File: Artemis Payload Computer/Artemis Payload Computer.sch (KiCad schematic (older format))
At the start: 0 parts

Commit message: complete redo hehe
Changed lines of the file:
@@
 $Descr A4 11693 8268
 encoding utf-8
-Sheet 1 2
+Sheet 1 6
 Title ""
 Date ""
@@
 Wire Wire Line
 	7450 1040 7220 1040
+$Sheet
+S 2400 2700 2650 1350
+U 60403E20
+F0 "Teensy3.2" 50
+F1 "Teensy3.sch" 50
+$EndSheet
+$Sheet
+S 5950 2700 1250 700
+U 60404056
+F0 "IMU" 50
+F1 "IMU.sch" 50
+$EndSheet
+$Sheet
+S 5950 3800 1250 650
+U 60404167
+F0 "BMP280" 50
+F1 "BMP280.sch" 50
+$EndSheet
+$Sheet
+S 6000 4950 1200 650
+U 60404A5A
+F0 "Power Supply" 50
+F1 "Power Supply.sch" 50
+$EndSheet
 $EndSCHEMATC

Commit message: ready for testing...
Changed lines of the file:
@@
 F0 "Teensy3.2" 50
 F1 "Teensy3.sch" 50
+F2 "SCL0" I R 5050 3100 50
+F3 "SDA0" I R 5050 3550 50
 $EndSheet
 $Sheet
@@
 F0 "IMU" 50
 F1 "IMU.sch" 50
+F2 "SCL0" I L 5950 2850 50
+F3 "SDA0" I L 5950 3150 50
 $EndSheet
 $Sheet
@@
 F0 "BMP280" 50
 F1 "BMP280.sch" 50
+F2 "SCL0" I L 5950 4000 50
+F3 "SDA0" I L 5950 4200 50
 $EndSheet
 $Sheet

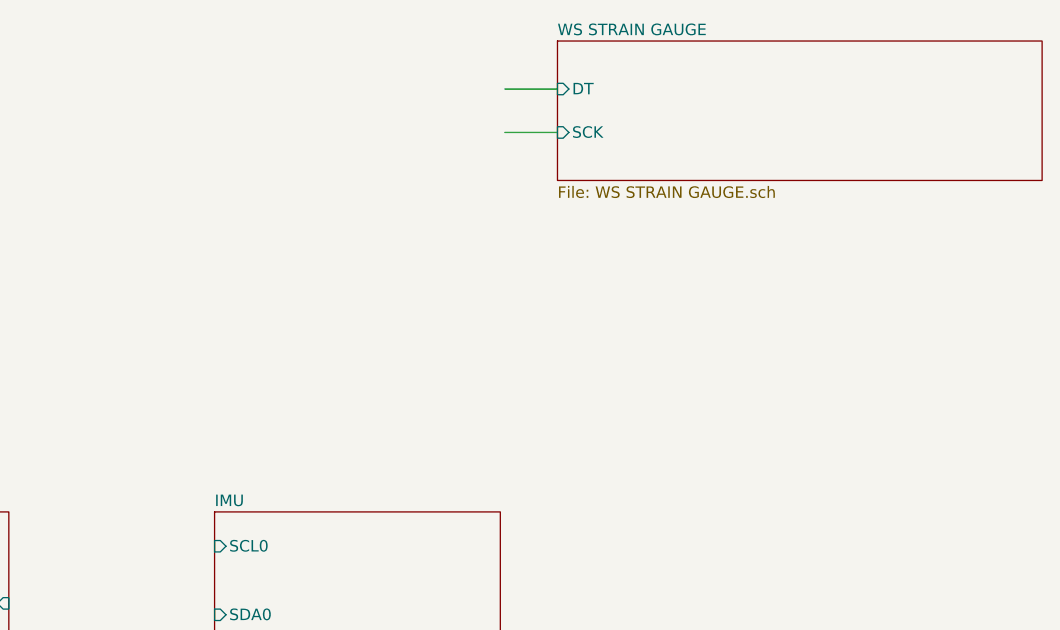
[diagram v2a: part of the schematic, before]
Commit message: Fixed Strain Gauge Footprint
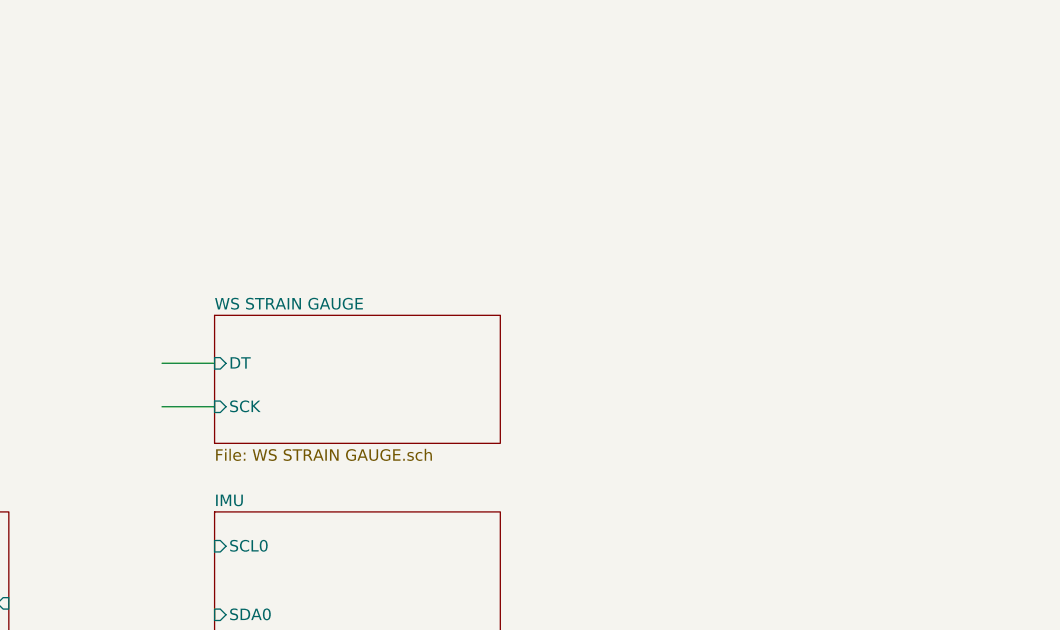
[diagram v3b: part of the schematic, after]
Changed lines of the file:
@@
 $EndDescr
 $Sheet
-S 7450 640  2120 610
+S 5950 1840 1250 560
 U 603A9D0E
 F0 "WS STRAIN GAUGE" 50
 F1 "WS STRAIN GAUGE.sch" 50
-F2 "DT" I L 7450 850 50
-F3 "SCK" I L 7450 1040 50
+F2 "DT" I L 5950 2050 50
+F3 "SCK" I L 5950 2240 50
 $EndSheet
 Wire Wire Line
-	7450 850  7220 850
+	5950 2050 5720 2050
 Wire Wire Line
-	7450 1040 7220 1040
+	5950 2240 5720 2240
 $Sheet
 S 2400 2700 2650 1350

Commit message: big commit, sorry. sd card needs finishing
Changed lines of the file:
@@
 $Descr A4 11693 8268
 encoding utf-8
-Sheet 1 6
+Sheet 1 7
 Title ""
 Date ""
@@
 F1 "Power Supply.sch" 50
 $EndSheet
+$Sheet
+S 8400 1800 1100 500
+U 604269F8
+F0 "SD_card" 50
+F1 "SD_card.sch" 50
+$EndSheet
 $EndSCHEMATC

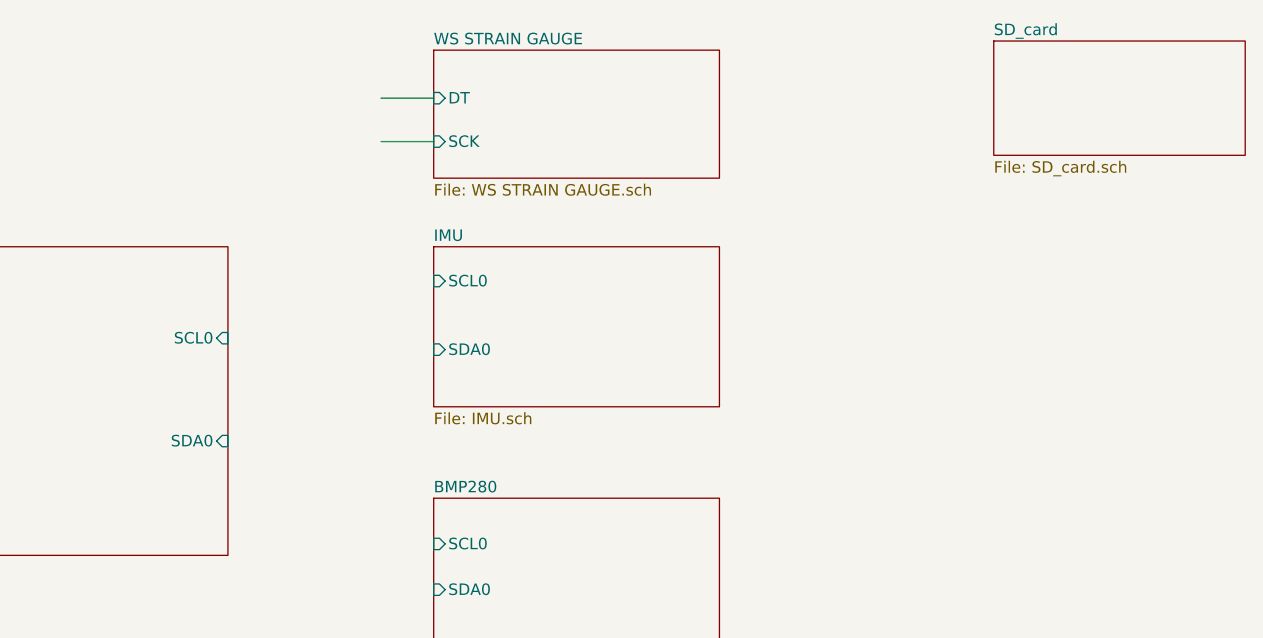
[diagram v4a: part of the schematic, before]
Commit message: Continued work on SD card. Starting PCB layout.
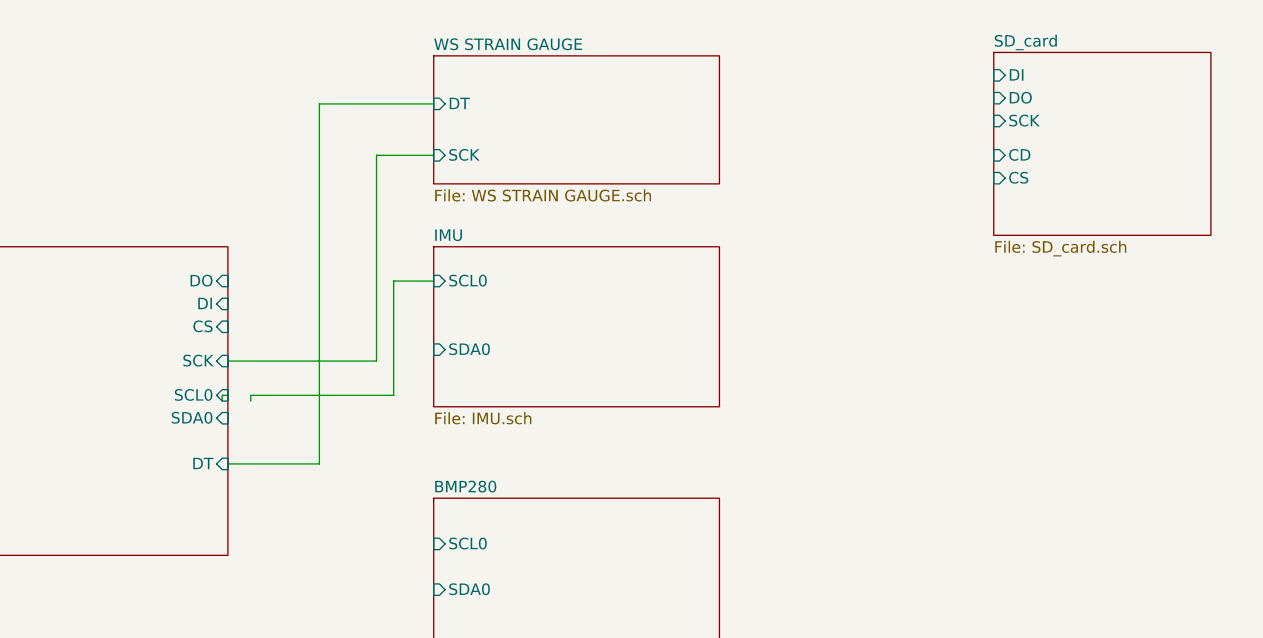
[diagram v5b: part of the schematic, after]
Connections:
- wire segments 2 -> 12
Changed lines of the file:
@@
 $EndDescr
 $Sheet
-S 5950 1840 1250 560
+S 5950 1865 1250 560
 U 603A9D0E
 F0 "WS STRAIN GAUGE" 50
 F1 "WS STRAIN GAUGE.sch" 50
-F2 "DT" I L 5950 2050 50
-F3 "SCK" I L 5950 2240 50
+F2 "DT" I L 5950 2075 50
+F3 "SCK" I L 5950 2300 50
 $EndSheet
-Wire Wire Line
-	5950 2050 5720 2050
-Wire Wire Line
-	5950 2240 5720 2240
 $Sheet
 S 2400 2700 2650 1350
@@
 F0 "Teensy3.2" 50
 F1 "Teensy3.sch" 50
-F2 "SCL0" I R 5050 3100 50
-F3 "SDA0" I R 5050 3550 50
+F2 "SCL0" I R 5050 3350 50
+F3 "SDA0" I R 5050 3450 50
+F4 "DO" I R 5050 2850 50
+F5 "DI" I R 5050 2950 50
+F6 "CS" I R 5050 3050 50
+F7 "SCK" I R 5050 3200 50
+F8 "DT" I R 5050 3650 50
 $EndSheet
 $Sheet
@@
 $EndSheet
 $Sheet
-S 8400 1800 1100 500
+S 8400 1850 950  800
 U 604269F8
 F0 "SD_card" 50
 F1 "SD_card.sch" 50
+F2 "CS" I L 8400 2400 50
+F3 "DI" I L 8400 1950 50
+F4 "SCK" I L 8400 2150 50
+F5 "DO" I L 8400 2050 50
+F6 "CD" I L 8400 2300 50
 $EndSheet
+Wire Wire Line
+	5450 2075 5950 2075
+Wire Wire Line
+	5050 3650 5450 3650
+Wire Wire Line
+	5700 3200 5050 3200
+Wire Wire Line
+	5450 2075 5450 3650
+Wire Wire Line
+	5950 2300 5700 2300
+Wire Wire Line
+	5700 2300 5700 3200
+Wire Wire Line
+	5950 2850 5775 2850
+Wire Wire Line
+	5775 2850 5775 3350
+Wire Wire Line
+	5150 3350 5150 3375
+Wire Wire Line
+	5025 3375 5025 3350
+Wire Wire Line
+	5025 3350 5050 3350
+Wire Wire Line
+	5150 3350 5775 3350
 $EndSCHEMATC

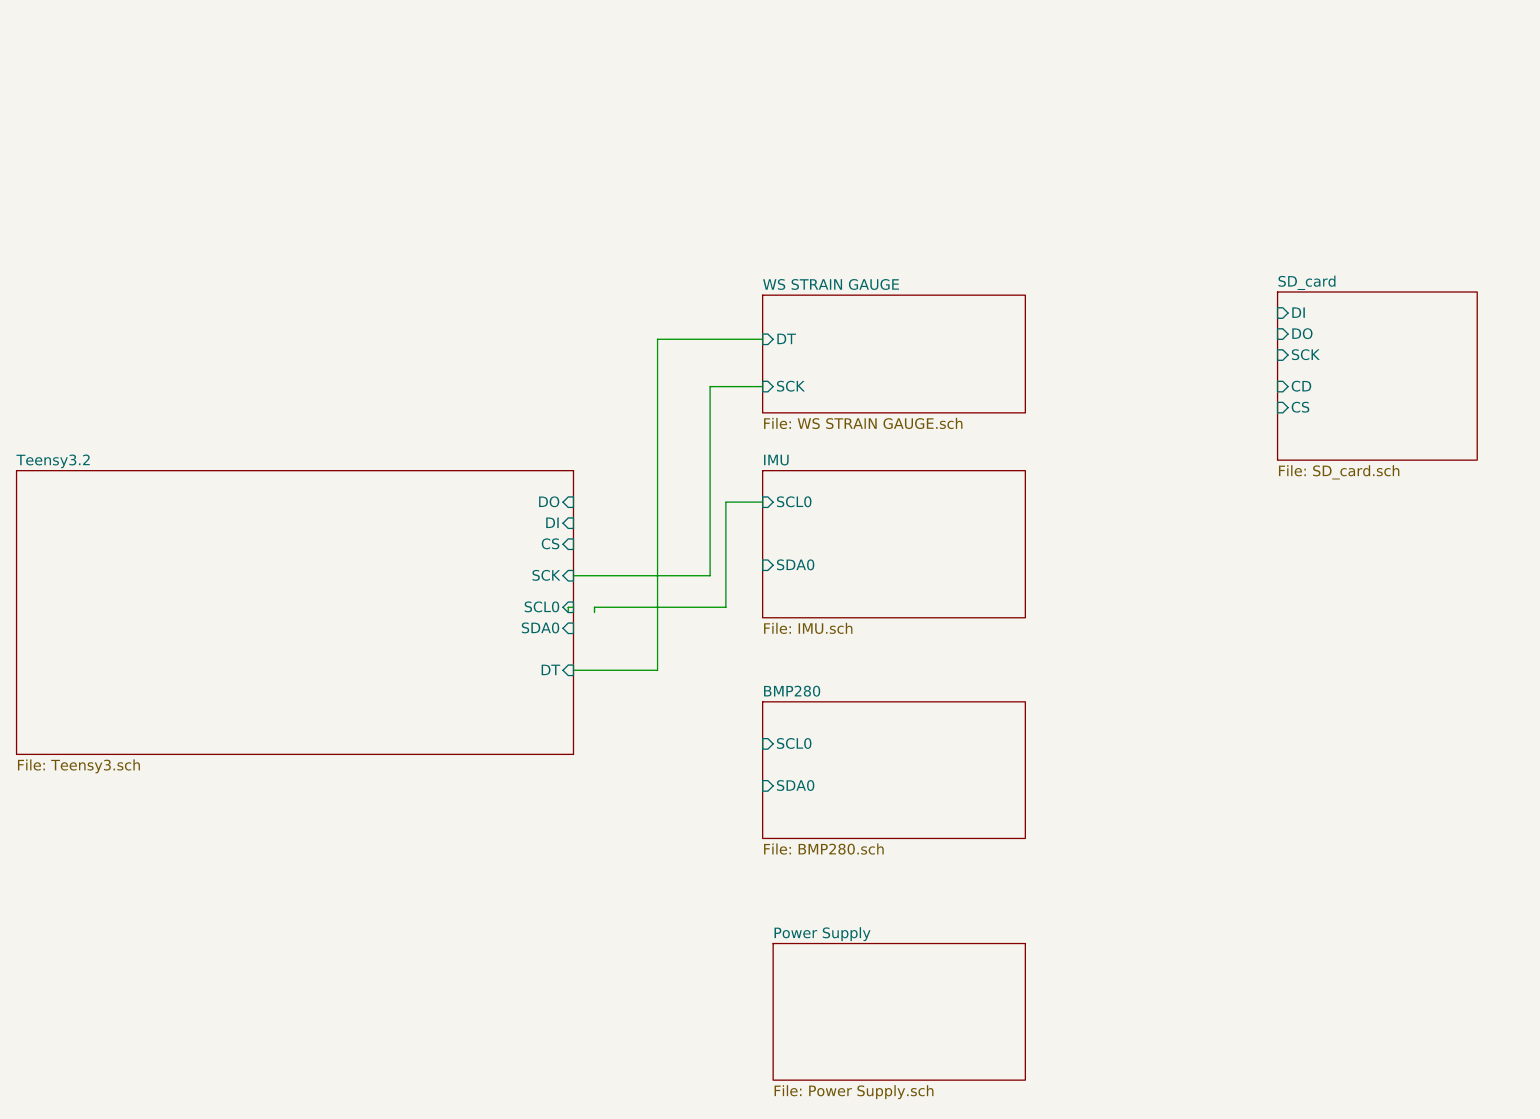
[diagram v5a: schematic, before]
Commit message: started tracing... they are bad
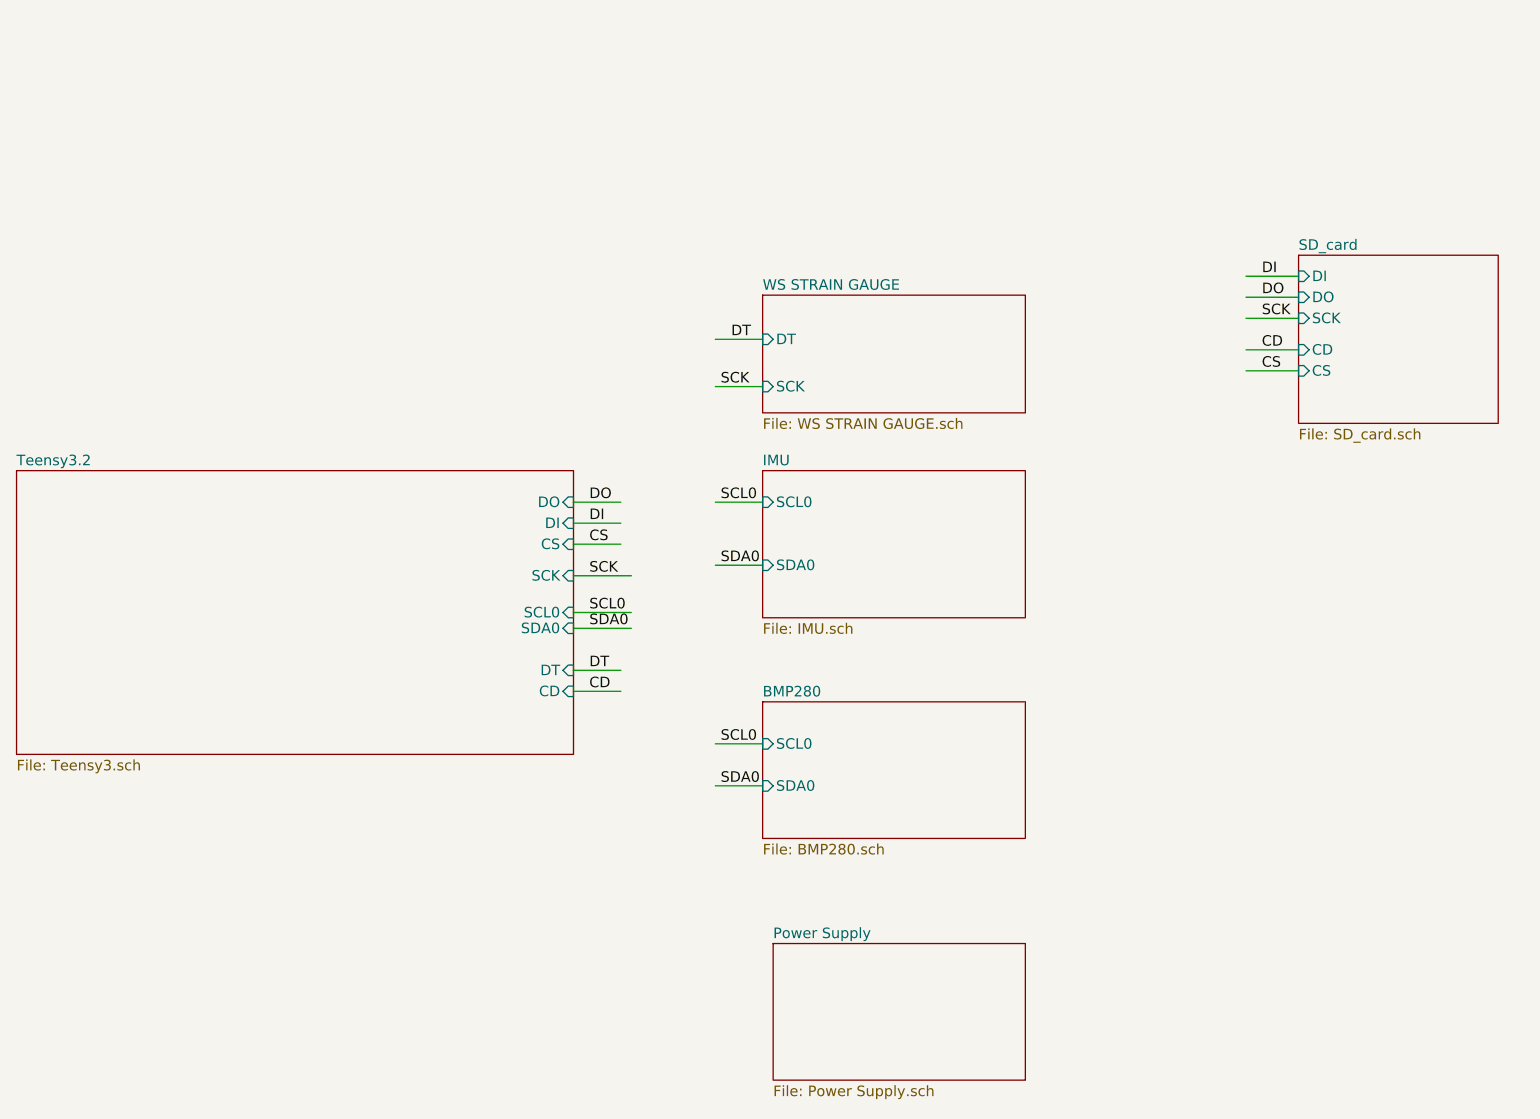
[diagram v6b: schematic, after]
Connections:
- net labels added: CD, CS, DI, DO, DT, SCK, SCL0, SDA0
- wire segments 12 -> 19
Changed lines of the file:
@@
-$EndSheet
-$Sheet
-S 2400 2700 2650 1350
-U 60403E20
-F0 "Teensy3.2" 50
-F1 "Teensy3.sch" 50
-F2 "SCL0" I R 5050 3350 50
-F3 "SDA0" I R 5050 3450 50
-F4 "DO" I R 5050 2850 50
-F5 "DI" I R 5050 2950 50
-F6 "CS" I R 5050 3050 50
-F7 "SCK" I R 5050 3200 50
-F8 "DT" I R 5050 3650 50
 $EndSheet
 $Sheet
@@
 $EndSheet
 $Sheet
-S 8400 1850 950  800
+S 8500 1675 950  800
 U 604269F8
 F0 "SD_card" 50
 F1 "SD_card.sch" 50
-F2 "CS" I L 8400 2400 50
-F3 "DI" I L 8400 1950 50
-F4 "SCK" I L 8400 2150 50
-F5 "DO" I L 8400 2050 50
-F6 "CD" I L 8400 2300 50
+F2 "CS" I L 8500 2225 50
+F3 "DI" I L 8500 1775 50
+F4 "SCK" I L 8500 1975 50
+F5 "DO" I L 8500 1875 50
+F6 "CD" I L 8500 2125 50
+$EndSheet
+$Sheet
+S 2400 2700 2650 1350
+U 60403E20
+F0 "Teensy3.2" 50
+F1 "Teensy3.sch" 50
+F2 "SCL0" I R 5050 3375 50
+F3 "SDA0" I R 5050 3450 50
+F4 "DO" I R 5050 2850 50
+F5 "DI" I R 5050 2950 50
+F6 "CS" I R 5050 3050 50
+F7 "SCK" I R 5050 3200 50
+F8 "DT" I R 5050 3650 50
+F9 "CD" I R 5050 3750 50
 $EndSheet
 Wire Wire Line
-	5450 2075 5950 2075
+	8500 1775 8250 1775
 Wire Wire Line
-	5050 3650 5450 3650
+	8500 1875 8250 1875
 Wire Wire Line
-	5700 3200 5050 3200
+	8500 1975 8250 1975
 Wire Wire Line
-	5450 2075 5450 3650
+	8500 2125 8250 2125
 Wire Wire Line
-	5950 2300 5700 2300
+	8500 2225 8250 2225
 Wire Wire Line
-	5700 2300 5700 3200
+	5950 2075 5725 2075
 Wire Wire Line
-	5950 2850 5775 2850
+	5950 2300 5725 2300
 Wire Wire Line
-	5775 2850 5775 3350
+	5950 2850 5725 2850
 Wire Wire Line
-	5150 3350 5150 3375
+	5950 3150 5725 3150
 Wire Wire Line
-	5025 3375 5025 3350
+	5950 4000 5725 4000
 Wire Wire Line
-	5025 3350 5050 3350
+	5950 4200 5725 4200
 Wire Wire Line
-	5150 3350 5775 3350
+	5050 2850 5275 2850
+Wire Wire Line
+	5050 2950 5275 2950
+Wire Wire Line
+	5050 3050 5275 3050
+Wire Wire Line
+	5050 3650 5275 3650
+Wire Wire Line
+	5050 3750 5275 3750
+Text Label 5125 2850 0    50   ~ 0
+DO
+Text Label 5125 2950 0    50   ~ 0
+DI
+Text Label 5125 3050 0    50   ~ 0
+CS
+Text Label 5125 3200 0    50   ~ 0
+SCK
+Text Label 5125 3375 0    50   ~ 0
+SCL0
+Text Label 5125 3450 0    50   ~ 0
+SDA0
+Text Label 5125 3650 0    50   ~ 0
+DT
+Text Label 5125 3750 0    50   ~ 0
+CD
+Wire Wire Line
+	5050 3375 5325 3375
+Wire Wire Line
+	5050 3450 5325 3450
+Wire Wire Line
+	5050 3200 5325 3200
+Text Label 5800 2075 0    50   ~ 0
+DT
+Text Label 5750 2300 0    50   ~ 0
+SCK
+Text Label 5750 2850 0    50   ~ 0
+SCL0
+Text Label 5750 3150 0    50   ~ 0
+SDA0
+Text Label 5750 4000 0    50   ~ 0
+SCL0
+Text Label 5750 4200 0    50   ~ 0
+SDA0
+Text Label 8325 1775 0    50   ~ 0
+DI
+Text Label 8325 1875 0    50   ~ 0
+DO
+Text Label 8325 1975 0    50   ~ 0
+SCK
+Text Label 8325 2125 0    50   ~ 0
+CD
+Text Label 8325 2225 0    50   ~ 0
+CS
 $EndSCHEMATC
